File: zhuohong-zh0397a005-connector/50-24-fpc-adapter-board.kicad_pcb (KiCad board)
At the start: 4 copper layers, 28.8 x 25.2 mm, 18 parts, among them J1 1-1734248-5, J2 10051922-2010ELF, SW1 SMD-BUTTON_4P-5.2X5.2X1.5MM-S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, U1 RS3236-2.5FY5, U3 AP3127B

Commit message: Fix names, footprints, and silkscreen of the pcb's
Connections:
- U3 pad 5: (no net) -> LEDA
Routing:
- net LEDA: track 6.91 -> 12.0 mm
- net CLK_C_P: track 17.1 -> 21.4 mm
- net CLK_C_N: track 17.1 -> 20.9 mm
- net LEDK: track 13.4 -> 14.5 mm, vias 0 -> 2
- net D0_P: track 17.5 -> 18.6 mm
- net D0_N: track 17.6 -> 18.6 mm
- added copper zone on B.Cu, net GND
- added copper zone on F.Cu, net GND

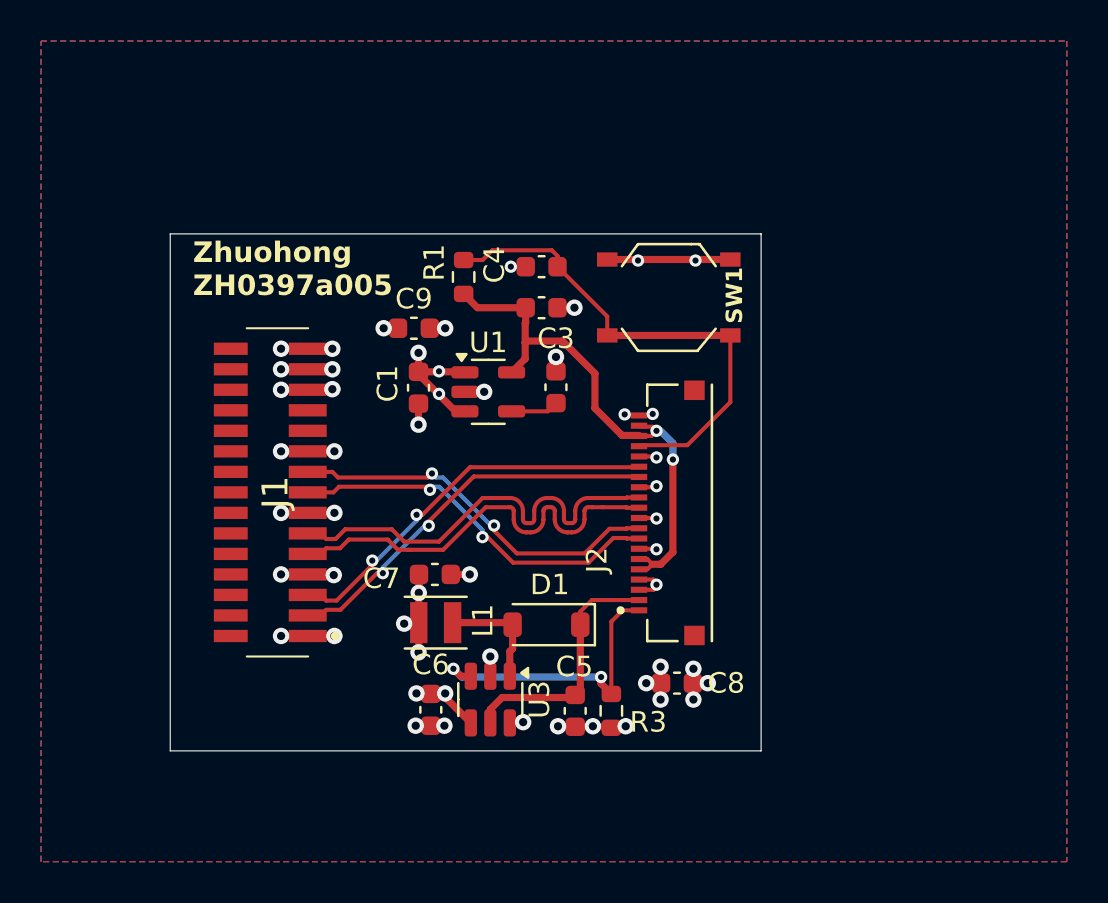
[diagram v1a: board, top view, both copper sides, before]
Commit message: Fixed lmt040wv004c board for production @ JLCPCB
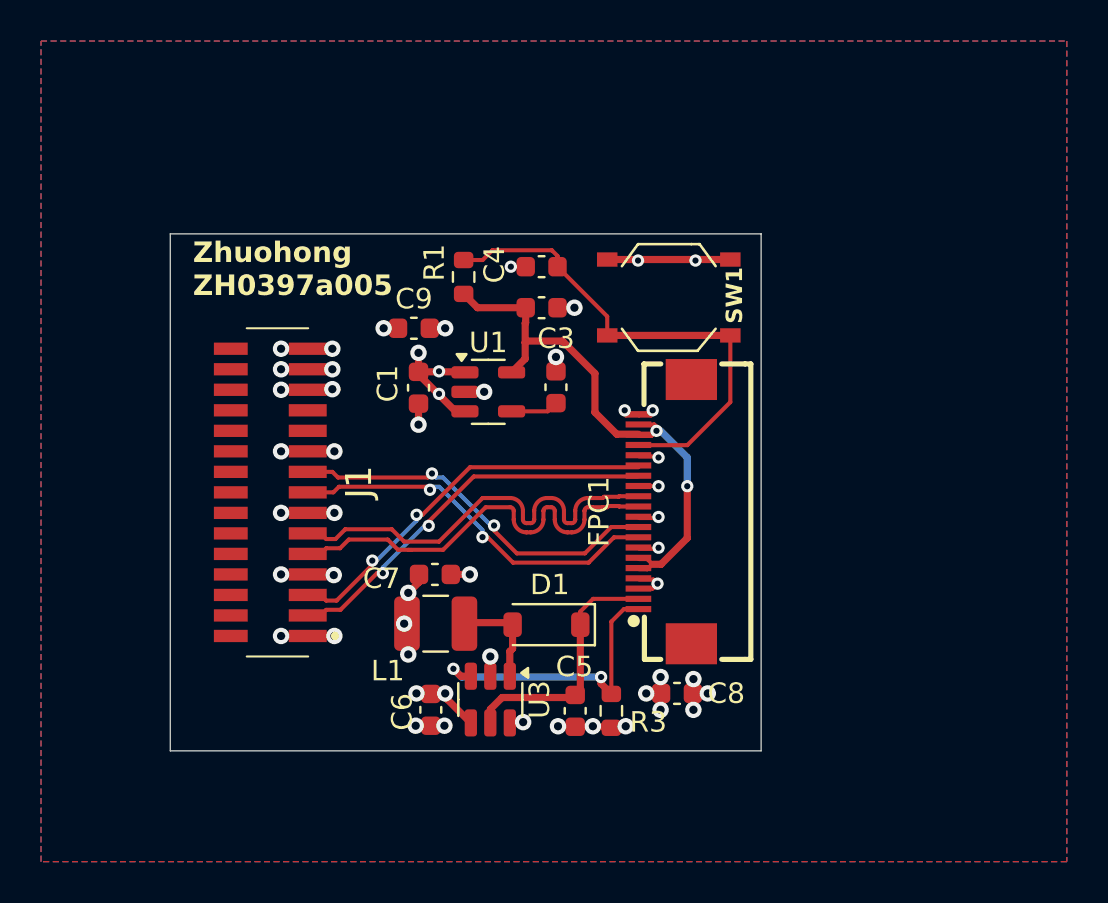
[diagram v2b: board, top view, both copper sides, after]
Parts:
- removed J2: 10051922-2010ELF, custom:AMPHENOL_10051922-2010ELF
- added FPC1: FPC-05F-20PH20, custom:FPC-SMD_20P-P0.50_XUNPU_FPC-05F-20PH20, F.Cu at (90.4, 62.9)
- L1: value 22uH -> 6.8uH; footprint Inductor_SMD:L_Changjiang_FNR252010S -> Inductor_SMD:L_1210_3225Metric
- R3: value 6R2 1% -> 5R0 5%
- U3: value AP3127B -> AP3032B
- moved C8 0.50 mm to (91.0, 71.8)
- moved L1 0.05 mm to (79.2, 68.4)
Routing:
- net +3V3: track 23.4 -> 22.2 mm
- net +2V8: track 26.0 -> 26.9 mm
- net GND: track 40.1 -> 40.9 mm
- net Net-(D1-A): track 5.39 -> 4.82 mm
